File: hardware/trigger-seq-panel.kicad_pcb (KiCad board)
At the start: 2 copper layers, 80.8 x 104.6 mm, 102 parts, among them J1 CLOCK_IN, J2 RESET, J3 DIRECTION, J4 OUT 1, J5 OUT 2, J6 CLOCK_OUT, J7 RUN/STOP, P2 COUNT_PANEL, P4 CLOCK_PANEL, P6 SWITCH_PANEL, P9 OUTS_PANEL, SW1 RESET, SW10 SWITCH_INV, SW11 SWITCH_INV, SW12 SWITCH_INV, SW13 SWITCH_INV, SW14 SWITCH_INV, SW15 SWITCH_INV, SW16 SWITCH_INV, SW17 SWITCH_INV, SW18 SWITCH_INV, SW19 SWITCH_INV, SW2 UP/DOWN, SW20 RUN/STOP, SW3 SW_DPDT_x2, SW4 SWITCH_INV, SW5 SWITCH_INV, SW6 SWITCH_INV, SW7 SWITCH_INV, SW8 SWITCH_INV, SW9 SWITCH_INV

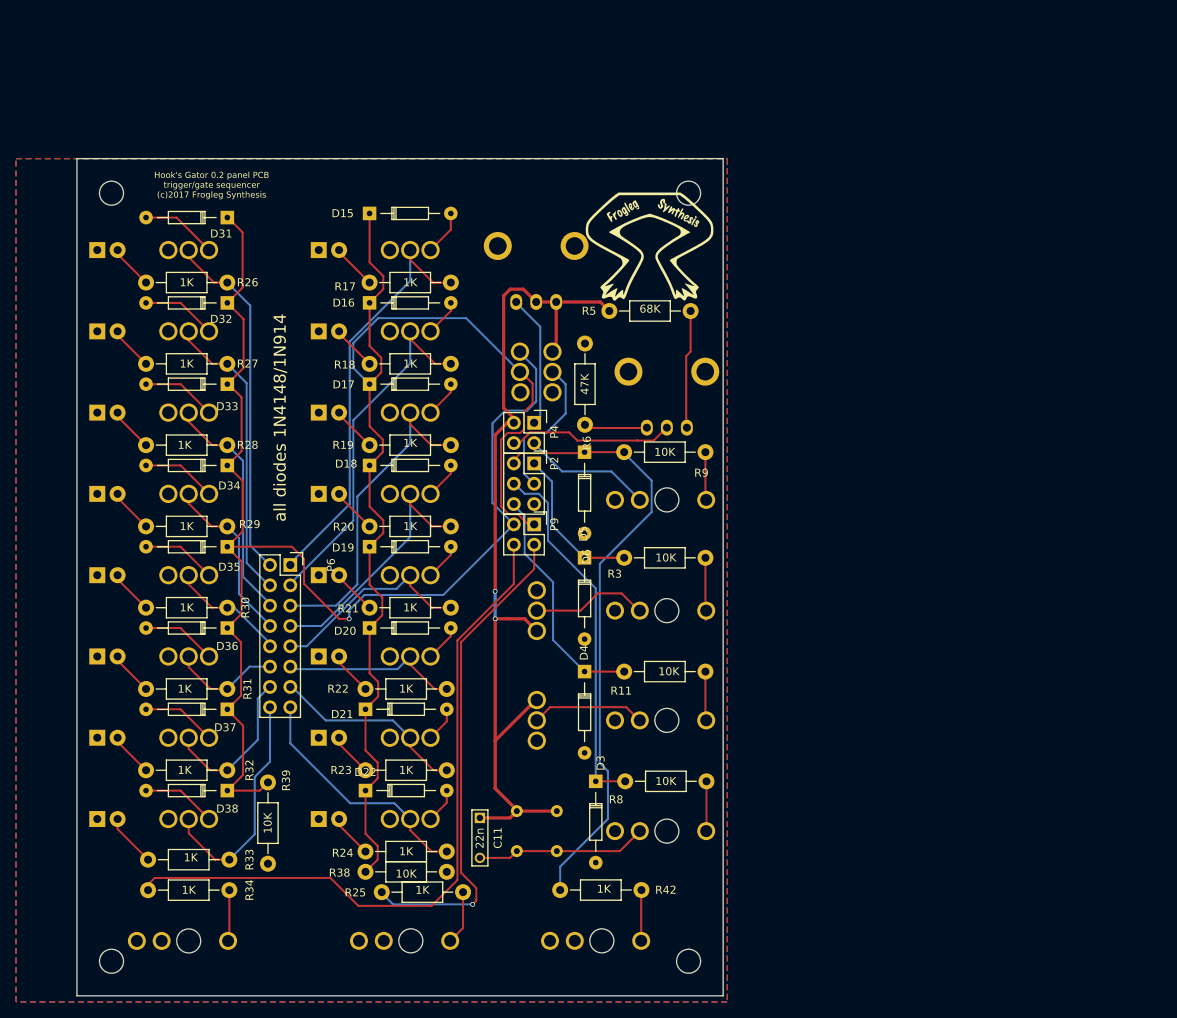
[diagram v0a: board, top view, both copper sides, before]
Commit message: replaced old hardware files with the most recent ones tracking CLAUDE.md AI files used in revising the project
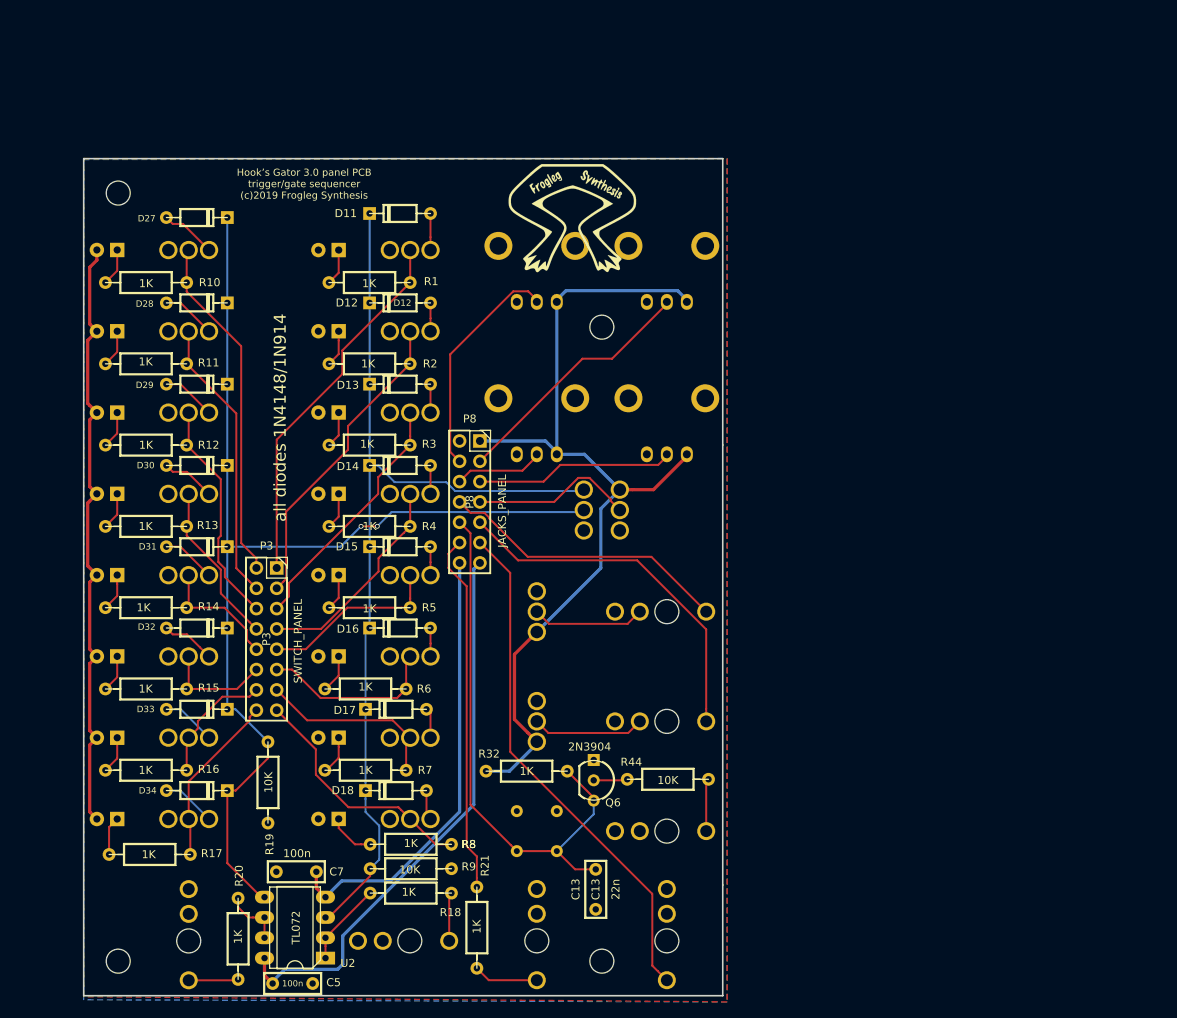
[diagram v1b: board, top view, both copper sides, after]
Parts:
- removed C11: 22n, Capacitors_ThroughHole:C_Rect_L7_W2_P5
- removed D35, D36, D37, D38: 1N4148, Diodes_ThroughHole:Diode_DO-35_SOD27_Horizontal_RM10
- removed P2: COUNT_PANEL, Socket_Strips:Socket_Strip_Straight_2x03
- removed P4: CLOCK_PANEL, Socket_Strips:Socket_Strip_Straight_2x02
- removed P6: SWITCH_PANEL, Socket_Strips:Socket_Strip_Straight_2x08
- removed P9: OUTS_PANEL, Socket_Strips:Socket_Strip_Straight_2x02
- removed R22, R23, R24, R25, R26, R27, R28, R29, R30, R31, R33, R34, R42: 1K, Resistors_ThroughHole:Resistor_Horizontal_RM10mm
- removed R38, R39: 10K, Resistors_ThroughHole:Resistor_Horizontal_RM10mm
- removed the SW14 at (86.8, 84.3)
- added C13: 22n, Capacitor_THT:C_Disc_D7.0mm_W2.5mm_P5.00mm, F.Cu at (137.7, 146.4)
- added C5: 100n, Capacitor_THT:C_Disc_D7.0mm_W2.5mm_P5.00mm, F.Cu at (97.3, 155.7)
- added C7: 100n, Capacitor_THT:C_Disc_D7.0mm_W2.5mm_P5.00mm, F.Cu at (102.7, 141.7)
- added P3: SWITCH_PANEL, Connector_PinSocket_2.54mm:PinSocket_2x08_P2.54mm_Vertical, F.Cu at (97.8, 103.8)
- added P8: JACKS_PANEL, Connector_PinSocket_2.54mm:PinSocket_2x07_P2.54mm_Vertical, F.Cu at (123.2, 87.9)
- added Q6: 2N3904, Package_TO_SOT_THT:TO-92_Inline_Wide, F.Cu at (137.4, 127.8)
- added R1: 1K, Resistor_THT:R_Axial_DIN0207_L6.3mm_D2.5mm_P10.16mm_Horizontal, F.Cu at (114.5, 68.1)
- added R10: 1K, Resistor_THT:R_Axial_DIN0207_L6.3mm_D2.5mm_P10.16mm_Horizontal, F.Cu at (86.5, 68.1)
- added R12: 1K, Resistor_THT:R_Axial_DIN0207_L6.3mm_D2.5mm_P10.16mm_Horizontal, F.Cu at (86.5, 88.4)
- added R13: 1K, Resistor_THT:R_Axial_DIN0207_L6.3mm_D2.5mm_P10.16mm_Horizontal, F.Cu at (86.5, 98.6)
- added R14: 1K, Resistor_THT:R_Axial_DIN0207_L6.3mm_D2.5mm_P10.16mm_Horizontal, F.Cu at (86.5, 108.7)
- added R15: 1K, Resistor_THT:R_Axial_DIN0207_L6.3mm_D2.5mm_P10.16mm_Horizontal, F.Cu at (86.5, 118.9)
- added R16: 1K, Resistor_THT:R_Axial_DIN0207_L6.3mm_D2.5mm_P10.16mm_Horizontal, F.Cu at (86.5, 129.0)
- added R2: 1K, Resistor_THT:R_Axial_DIN0207_L6.3mm_D2.5mm_P10.16mm_Horizontal, F.Cu at (114.5, 78.2)
- added R4: 1K, Resistor_THT:R_Axial_DIN0207_L6.3mm_D2.5mm_P10.16mm_Horizontal, F.Cu at (114.5, 98.6)
- added R44: 10K, Resistor_THT:R_Axial_DIN0207_L6.3mm_D2.5mm_P10.16mm_Horizontal, F.Cu at (141.6, 130.2)
- added R7: 1K, Resistor_THT:R_Axial_DIN0207_L6.3mm_D2.5mm_P10.16mm_Horizontal, F.Cu at (114.0, 129.0)
- added RV3: STEPS, Walter Resistors:trimmer_alps-rk09k1130ah1, B.Cu at (146.6, 82.5)
- added RV4: SWING, Walter Resistors:trimmer_alps-rk09k1130ah1, B.Cu at (130.3, 82.5)
- added SW16: SW_SPDT, My Library:submini_toggle_SPDT_2267079, B.Cu at (86.8, 125.0)
- added U2: TL072, Package_DIP:DIP-8_W7.62mm_LongPads, F.Cu at (103.9, 152.5)
- D10: value S4 -> S8; footprint LEDs:LED-3MM -> My Library:LED_D3.0mm
- D11: value S5 -> 1N4148; footprint LEDs:LED-3MM -> Diode_THT:D_DO-35_SOD27_P7.62mm_Horizontal; moved to F.Cu
- D12: value S6 -> 1N4148; footprint LEDs:LED-3MM -> Diode_THT:D_DO-35_SOD27_P7.62mm_Horizontal; moved to F.Cu
- D13: value S7 -> 1N4148; footprint LEDs:LED-3MM -> Diode_THT:D_DO-35_SOD27_P7.62mm_Horizontal; moved to F.Cu
- D14: value S8 -> 1N4148; footprint LEDs:LED-3MM -> Diode_THT:D_DO-35_SOD27_P7.62mm_Horizontal; moved to F.Cu
- D15, D16, D17, D18, D31, D32, D33, D34: footprint Diodes_ThroughHole:Diode_DO-35_SOD27_Horizontal_RM10 -> Diode_THT:D_DO-35_SOD27_P7.62mm_Horizontal
- D19: value 1N4148 -> S9; footprint Diodes_ThroughHole:Diode_DO-35_SOD27_Horizontal_RM10 -> My Library:LED_D3.0mm; moved to B.Cu
- D20: value 1N4148 -> S10; footprint Diodes_ThroughHole:Diode_DO-35_SOD27_Horizontal_RM10 -> My Library:LED_D3.0mm; moved to B.Cu
- D21: value 1N4148 -> S11; footprint Diodes_ThroughHole:Diode_DO-35_SOD27_Horizontal_RM10 -> My Library:LED_D3.0mm; moved to B.Cu
- D22: value 1N4148 -> S12; footprint Diodes_ThroughHole:Diode_DO-35_SOD27_Horizontal_RM10 -> My Library:LED_D3.0mm; moved to B.Cu
- D23: value S9 -> S13; footprint LEDs:LED-3MM -> My Library:LED_D3.0mm
- D24: value S10 -> S14; footprint LEDs:LED-3MM -> My Library:LED_D3.0mm
- D25: value S11 -> S15; footprint LEDs:LED-3MM -> My Library:LED_D3.0mm
- D26: value S12 -> S16; footprint LEDs:LED-3MM -> My Library:LED_D3.0mm
- D27: value S13 -> 1N4148; footprint LEDs:LED-3MM -> Diode_THT:D_DO-35_SOD27_P7.62mm_Horizontal; moved to F.Cu
- D28: value S14 -> 1N4148; footprint LEDs:LED-3MM -> Diode_THT:D_DO-35_SOD27_P7.62mm_Horizontal; moved to F.Cu
- D29: value S15 -> 1N4148; footprint LEDs:LED-3MM -> Diode_THT:D_DO-35_SOD27_P7.62mm_Horizontal; moved to F.Cu
- D3: value 1N4148 -> S1; footprint Diodes_ThroughHole:Diode_DO-35_SOD27_Horizontal_RM10 -> My Library:LED_D3.0mm; moved to B.Cu
- D30: value S16 -> 1N4148; footprint LEDs:LED-3MM -> Diode_THT:D_DO-35_SOD27_P7.62mm_Horizontal; moved to F.Cu
- D4: value 1N4148 -> S2; footprint Diodes_ThroughHole:Diode_DO-35_SOD27_Horizontal_RM10 -> My Library:LED_D3.0mm; moved to B.Cu
- D5: value 1N4148 -> S3; footprint Diodes_ThroughHole:Diode_DO-35_SOD27_Horizontal_RM10 -> My Library:LED_D3.0mm; moved to B.Cu
- D6: value 1N4148 -> S4; footprint Diodes_ThroughHole:Diode_DO-35_SOD27_Horizontal_RM10 -> My Library:LED_D3.0mm; moved to B.Cu
- D7: value S1 -> S5; footprint LEDs:LED-3MM -> My Library:LED_D3.0mm
- D8: value S2 -> S6; footprint LEDs:LED-3MM -> My Library:LED_D3.0mm
- D9: value S3 -> S7; footprint LEDs:LED-3MM -> My Library:LED_D3.0mm
- J1: value CLOCK_IN -> OUT1
- J2: value RESET -> OUT2
- J3: value DIRECTION -> RESET
- J4: value OUT 1 -> CLOCK_IN
- J5: value OUT 2 -> RUN_STOP
- J6: value CLOCK_OUT -> UP_DOWN
- J7: value RUN/STOP -> CLOCK_OUT
- R11, R3, R8: value 10K -> 1K; footprint Resistors_ThroughHole:Resistor_Horizontal_RM10mm -> Resistor_THT:R_Axial_DIN0207_L6.3mm_D2.5mm_P10.16mm_Horizontal
- R17, R18, R20, R21, R32, R9: footprint Resistors_ThroughHole:Resistor_Horizontal_RM10mm -> Resistor_THT:R_Axial_DIN0207_L6.3mm_D2.5mm_P10.16mm_Horizontal
- R19: value 1K -> 10K; footprint Resistors_ThroughHole:Resistor_Horizontal_RM10mm -> Resistor_THT:R_Axial_DIN0207_L6.3mm_D2.5mm_P10.16mm_Horizontal
- R5: value 68K -> 1K; footprint Resistors_ThroughHole:Resistor_Horizontal_RM10mm -> Resistor_THT:R_Axial_DIN0207_L6.3mm_D2.5mm_P10.16mm_Horizontal
- R6: value 47K -> 1K; footprint Resistors_ThroughHole:Resistor_Horizontal_RM10mm -> Resistor_THT:R_Axial_DIN0207_L6.3mm_D2.5mm_P10.16mm_Horizontal
- RV1: value 100K -> RATE
- RV2: value 100K -> WIDTH
- SW1: value RESET -> SW_SPDT; footprint My Library:C&K_round_pushbutton -> My Library:submini_toggle_SPDT_2267079
- SW10, SW11, SW12, SW13, SW15, SW17, SW4, SW5, SW6, SW7, SW8: value SWITCH_INV -> SW_SPDT
- SW14: renamed from SW16; value SWITCH_INV -> SW_SPDT
- SW18: value SWITCH_INV -> Run/Stop
- SW19: value SWITCH_INV -> Up/Down
- SW2: value UP/DOWN -> SW_SPDT
- SW20: value RUN/STOP -> RESET; footprint My Library:submini_toggle_SPDT_2267079 -> My Library:C&K_round_pushbutton
- SW3: value SW_DPDT_x2 -> SW_SPDT; footprint My Library:submini_toggle_DPDT_2267079 -> My Library:submini_toggle_SPDT_2267079
- SW9: value SWITCH_INV -> SW_DPDT_x2; footprint My Library:submini_toggle_SPDT_2267079 -> My Library:submini_toggle_DPDT_wider
- moved R17 76.6 mm to (87.0, 139.6)
- moved SW1 74.3 mm to (114.5, 64.0), turned to -90 degrees
- moved D3 74.3 mm to (104.3, 64.0), turned to 0 degrees
- moved J5 72.6 mm to (146.6, 109.2)
- moved SW10 67.0 mm to (86.8, 64.0)
- moved SW11 67.0 mm to (86.8, 74.2)
- moved R11 66.9 mm to (86.5, 78.2), turned to 180 degrees
- moved R18 66.4 mm to (119.6, 144.4)
- moved J1 63.8 mm to (114.4, 150.4)
- moved J2 61.3 mm to (86.8, 150.4), turned to 0 degrees
- moved R20 60.6 mm to (93.0, 155.2), turned to 90 degrees
- moved R9 56.4 mm to (119.6, 141.4), turned to 180 degrees
- moved D4 53.2 mm to (104.3, 74.2), turned to 0 degrees
- moved SW2 51.1 mm to (114.5, 74.2), turned to -90 degrees
- moved R19 50.5 mm to (96.7, 135.6), turned to 90 degrees
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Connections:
- D11 pad 1: GND -> Net-(D11-Pad1)
- D12 pad 1: GND -> Net-(D11-Pad1)
- D13 pad 1: GND -> Net-(D11-Pad1)
- D14 pad 1: GND -> Net-(D11-Pad1)
- D15 pad 1: /main/counter/1ST8 -> Net-(D11-Pad1)
- D16 pad 1: /main/counter/1ST8 -> Net-(D11-Pad1)
- D17 pad 1: /main/counter/1ST8 -> Net-(D11-Pad1)
- D18 pad 1: /main/counter/1ST8 -> Net-(D11-Pad1)
- D19 pad 1: /main/counter/1ST8 -> GND
- D20 pad 1: /main/counter/1ST8 -> GND
- D21 pad 1: /main/counter/1ST8 -> GND
- D22 pad 1: /main/counter/1ST8 -> GND
- D27 pad 1: GND -> Net-(D27-Pad1)
- D28 pad 1: GND -> Net-(D27-Pad1)
- D29 pad 1: GND -> Net-(D27-Pad1)
- D3 pad 1: /main/counter/reset processing/reset.in -> GND
- D3 pad 2: GND -> Net-(D3-Pad2)
- D30 pad 1: GND -> Net-(D27-Pad1)
- D31 pad 1: /main/counter/2ND8 -> Net-(D27-Pad1)
- D32 pad 1: /main/counter/2ND8 -> Net-(D27-Pad1)
- D33 pad 1: /main/counter/2ND8 -> Net-(D27-Pad1)
- D34 pad 1: /main/counter/2ND8 -> Net-(D27-Pad1)
- D4 pad 1: Net-(D4-Pad1) -> GND
- D4 pad 2: GND -> Net-(D4-Pad2)
- D5 pad 1: Net-(D5-Pad1) -> GND
- D5 pad 2: GND -> Net-(D5-Pad2)
- D6 pad 1: /main/counter/PROC_CLK -> GND
- D6 pad 2: GND -> Net-(D6-Pad2)
- J1 pad 2: /main/clock/INT_CLK -> (no net)
- J2 pad 2: Net-(C11-Pad2) -> (no net)
- J3 pad 2: Net-(J3-Pad2) -> GND
- J4 pad 1: Net-(J4-Pad1) -> CKIN
- J4 pad 2: (no net) -> GND
- J5 pad 1: Net-(J5-Pad1) -> R/S
- J5 pad 2: (no net) -> Net-(J5-Pad2)
- J6 pad 1: Net-(J6-Pad1) -> U/D
- J6 pad 2: (no net) -> Net-(J6-Pad2)
- J7 pad 2: Net-(J7-Pad2) -> (no net)
- R11 pad 1: Net-(D4-Pad1) -> /main/outputs/S10
- R11 pad 2: Net-(J3-Pad1) -> Net-(D20-Pad2)
- R17 pad 1: /main/counter/S1 -> /main/outputs/S16
- R17 pad 2: Net-(D7-Pad2) -> Net-(D26-Pad2)
- R18 pad 1: /main/counter/S2 -> Net-(J1-Pad1)
- R18 pad 2: Net-(D8-Pad2) -> Net-(R18-Pad2)
- R19 pad 1: /main/counter/S3 -> GND
- R19 pad 2: Net-(D9-Pad2) -> Net-(D27-Pad1)
- R20 pad 1: /main/counter/S4 -> Net-(J2-Pad1)
- R20 pad 2: Net-(D10-Pad2) -> Net-(R20-Pad2)
- R21 pad 1: /main/counter/S5 -> /main/clock/ckbuf
- R21 pad 2: Net-(D11-Pad2) -> Net-(J7-Pad1)
- R3 pad 1: Net-(D5-Pad1) -> /main/outputs/S3
- R3 pad 2: Net-(J7-Pad1) -> Net-(D5-Pad2)
- R32 pad 1: /main/counter/S15 -> +5V
- R32 pad 2: Net-(D29-Pad2) -> reset
- R5 pad 1: Net-(R5-Pad1) -> /main/outputs/S5
- R5 pad 2: +12V -> Net-(D7-Pad2)
- R6 pad 1: GND -> /main/outputs/S6
- R6 pad 2: Net-(R6-Pad2) -> Net-(D8-Pad2)
- R8 pad 1: /main/counter/reset processing/reset.in -> /main/outputs/S8
- R8 pad 2: Net-(J2-Pad1) -> Net-(D10-Pad2)
- R9 pad 1: /main/counter/PROC_CLK -> GND
- R9 pad 2: Net-(J1-Pad1) -> Net-(D11-Pad1)
- RV1 pad 1: +12V -> +5V
- RV1 pad 2: +12V -> rate
- RV1 pad 3: Net-(P4-Pad1) -> GND
- RV2 pad 1: Net-(R5-Pad1) -> +5V
- RV2 pad 2: Net-(P4-Pad4) -> width
- RV2 pad 3: Net-(R6-Pad2) -> GND
- SW1 pad 1: Net-(C11-Pad2) -> Net-(D11-Pad2)
- SW1 pad 2: +12V -> /main/outputs/S1
- SW10 pad 1: Net-(D21-Pad2) -> Net-(D27-Pad2)
- SW10 pad 2: /main/counter/S7 -> /main/outputs/S9
- SW11 pad 1: Net-(D22-Pad2) -> Net-(D28-Pad2)
- SW11 pad 2: /main/counter/S8 -> /main/outputs/S10
- SW12 pad 1: Net-(D31-Pad2) -> Net-(D29-Pad2)
- SW12 pad 2: /main/counter/S9 -> /main/outputs/S11
- SW13 pad 1: Net-(D32-Pad2) -> Net-(D30-Pad2)
- SW13 pad 2: /main/counter/S10 -> /main/outputs/S12
- SW14 pad 1: Net-(D35-Pad2) -> Net-(D31-Pad2)
- SW14 pad 2: /main/counter/S13 -> /main/outputs/S13
- SW15 pad 1: Net-(D34-Pad2) -> Net-(D32-Pad2)
- SW15 pad 2: /main/counter/S12 -> /main/outputs/S14
- SW17 pad 1: Net-(D36-Pad2) -> Net-(D34-Pad2)
- SW17 pad 2: /main/counter/S14 -> /main/outputs/S16
- SW18 pad 1: Net-(D37-Pad2) -> GND
- SW18 pad 2: /main/counter/S15 -> Net-(J5-Pad2)
- SW18 pad 3: (no net) -> +5V
- SW19 pad 1: Net-(D38-Pad2) -> +5V
- SW19 pad 2: /main/counter/S16 -> Net-(J6-Pad2)
- SW19 pad 3: (no net) -> GND
- SW2 pad 1: GND -> Net-(D12-Pad2)
- SW2 pad 2: Net-(J3-Pad2) -> /main/outputs/S2
- SW2 pad 3: +12V -> (no net)
- SW20 pad 1: GND -> reset
- SW20 pad 2: Net-(J7-Pad2) -> GND
- SW3 pad 1: +12V -> Net-(D13-Pad2)
- SW3 pad 2: Net-(P2-Pad3) -> /main/outputs/S3
- SW3 pad 3: GND -> (no net)
- SW4 pad 1: Net-(D15-Pad2) -> Net-(D14-Pad2)
- SW4 pad 2: /main/counter/S1 -> /main/outputs/S4
- SW5 pad 1: Net-(D16-Pad2) -> Net-(D15-Pad2)
- SW5 pad 2: /main/counter/S2 -> /main/outputs/S5
- SW6 pad 1: Net-(D17-Pad2) -> Net-(D16-Pad2)
- SW6 pad 2: /main/counter/S3 -> /main/outputs/S6
- SW7 pad 1: Net-(D18-Pad2) -> Net-(D17-Pad2)
- SW7 pad 2: /main/counter/S4 -> /main/outputs/S7
- SW8 pad 1: Net-(D19-Pad2) -> Net-(D18-Pad2)
- SW8 pad 2: /main/counter/S5 -> /main/outputs/S8
- SW9 pad 1: Net-(D20-Pad2) -> +5V
- SW9 pad 2: /main/counter/S6 -> 2x8/1x16
- SW9 pad 3: (no net) -> GND
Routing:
- net /main/counter/2ND8: track 162.4 -> 0.00 mm, vias 1 -> 0
- net /main/counter/1ST8: track 148.5 -> 0.00 mm
- net Net-(D27-Pad1): track 0.00 -> 139.0 mm, vias 0 -> 2
- net Net-(D11-Pad1): track 0.00 -> 120.1 mm
- net +5V: track 0.00 -> 113.2 mm
- net Net-(P10-Pad4): track 87.3 -> 0.00 mm
- net /main/counter/PROC_CLK: track 77.1 -> 0.00 mm
- net GND: track 0.00 -> 76.8 mm
- net reset: track 0.00 -> 68.2 mm
- net CKIN: track 0.00 -> 64.4 mm
- net Net-(P10-Pad3): track 61.8 -> 0.00 mm, vias 1 -> 0
- net -12V: track 0.00 -> 55.8 mm
- net /main/counter/S1: track 53.0 -> 0.00 mm
- net /main/counter/reset processing/reset.in: track 46.9 -> 0.00 mm
- net /main/outputs/S1: track 0.00 -> 46.7 mm
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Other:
- board size 80.8 x 104.6 mm -> 79.9 x 104.6 mm
- net class Default removed
- net class power removed
- board text added: "Hook’s Gator 3.0 panel PCB trigger/gate sequencer (c)2019 Frogleg Synthesis"
- board text added: "all pots 10kB"
- board text added: "steps"
- board text added: "swing"
- board text removed: "Hook's Gator 0.2 panel PCB trigger/gate sequencer (c)2017 Frogleg Synthesis"

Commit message: expanding panel to 18HP so the controls are less crowded
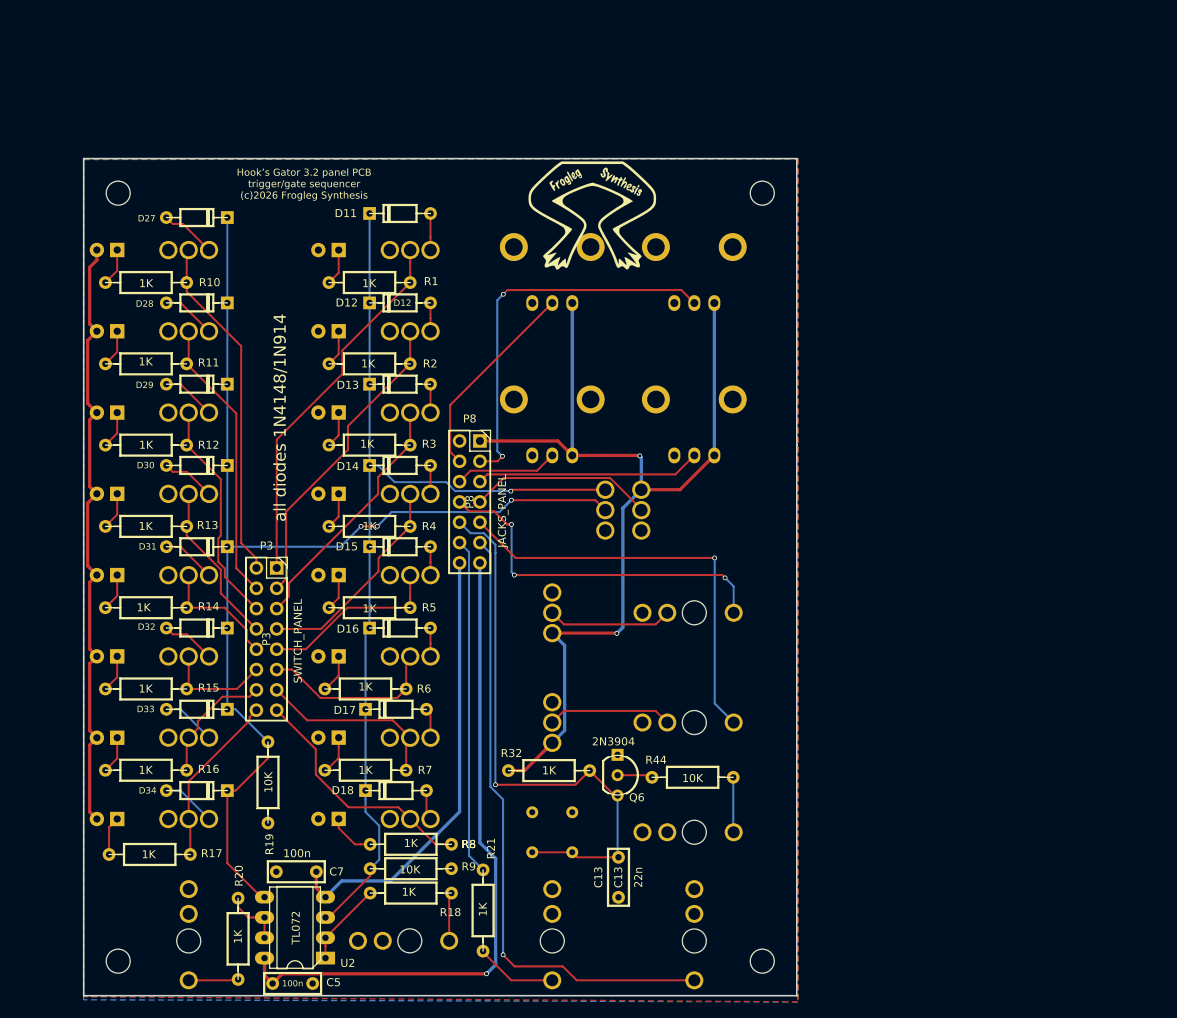
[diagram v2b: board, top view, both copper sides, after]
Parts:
- moved REF** 26.1 mm to (158.5, 56.9)
- moved REF** 20.1 mm to (158.5, 152.9)
- moved RV3 3.44 mm to (150.0, 82.7)
- moved J3 3.44 mm to (150.0, 136.8)
- moved J5 3.44 mm to (150.0, 109.4)
- moved RV2 3.44 mm to (150.0, 63.6)
- moved J6 3.44 mm to (150.0, 123.1)
- moved J4 3.43 mm to (150.0, 150.4)
- moved C13 3.22 mm to (140.5, 144.9)
- moved R44 3.10 mm to (144.7, 129.9)
- moved Q6 3.05 mm to (140.4, 127.1)
- moved R32 2.80 mm to (126.8, 129.1)
- moved SW9 2.68 mm to (141.1, 96.5)
- moved G*** 2.52 mm to (137.2, 60.4)
- moved R21 2.28 mm to (123.6, 141.5)
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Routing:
- net width: track 31.8 -> 48.7 mm, vias 0 -> 2
- net CKIN: track 64.4 -> 78.0 mm, vias 0 -> 1
- net +12V: track 70.5 -> 83.3 mm, vias 0 -> 1
- net +5V: track 113.2 -> 123.3 mm, vias 0 -> 2
- net R/S: track 36.6 -> 45.4 mm, vias 0 -> 3
- net U/D: track 45.3 -> 52.8 mm, vias 0 -> 1
- net Net-(D27-Pad1): track 139.0 -> 142.7 mm, vias 2 -> 3
- net reset: track 68.2 -> 71.7 mm, vias 0 -> 1
- net steps: track 24.9 -> 28.2 mm
- net rate: track 28.6 -> 25.6 mm
- net /main/clock/ckbuf: track 45.1 -> 42.1 mm
- net Net-(D11-Pad1): track 120.1 -> 122.8 mm, vias 0 -> 1
- net 2x8/1x16: track 20.5 -> 23.1 mm
- net Net-(J7-Pad1): track 8.11 -> 10.2 mm
- net swing: track 11.2 -> 12.9 mm
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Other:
- board size 79.9 x 104.6 mm -> 89.1 x 104.6 mm
- board text added: "Hook’s Gator 3.2 panel PCB trigger/gate sequencer (c)2026 Frogleg Synthesis"
- board text removed: "Hook’s Gator 3.0 panel PCB trigger/gate sequencer (c)2019 Frogleg Synthesis"

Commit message: wider panel + better spacing v3.3
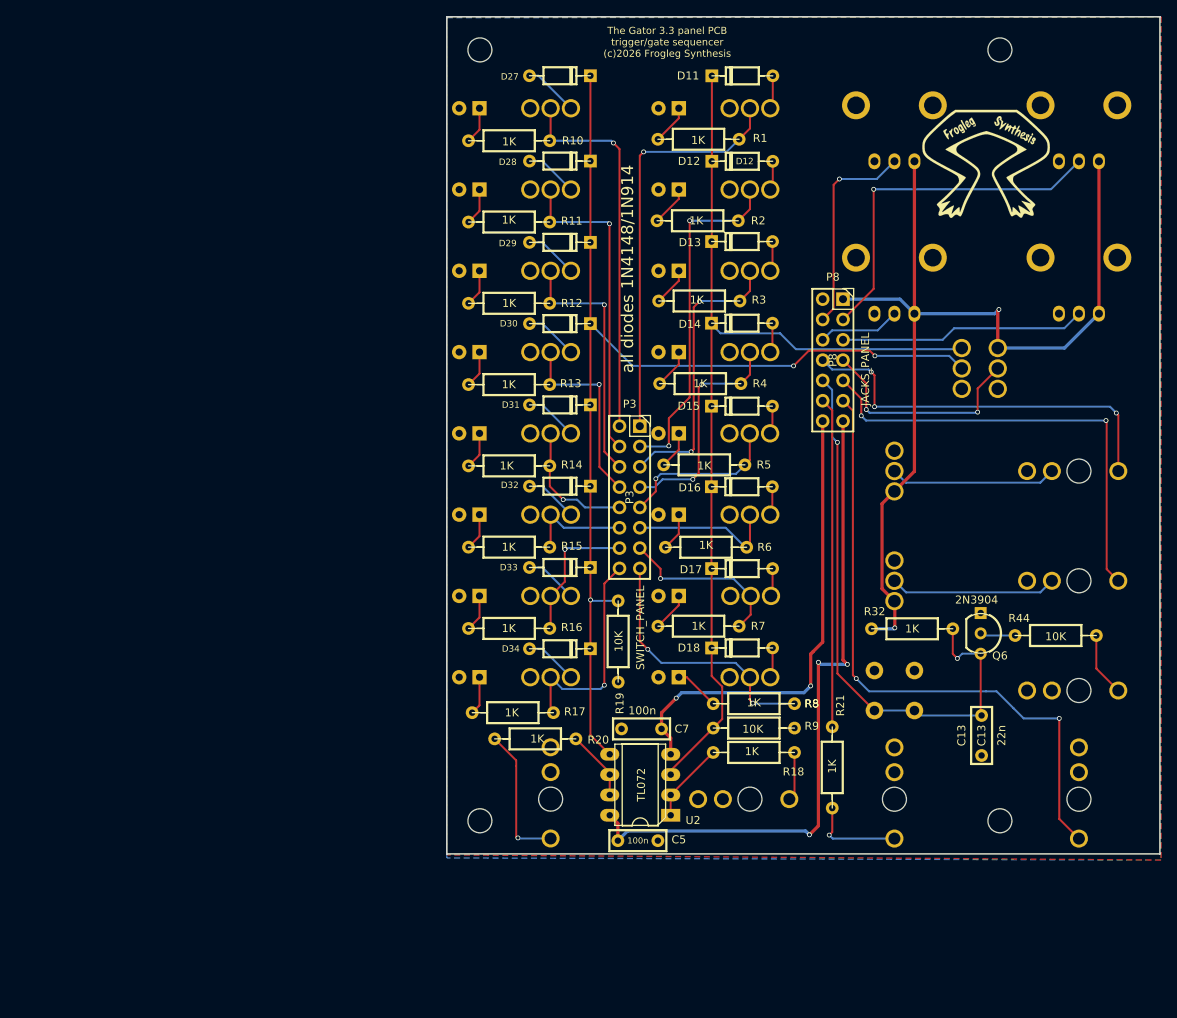
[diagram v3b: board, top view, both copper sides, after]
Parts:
- SW20: footprint My Library:C&K_round_pushbutton -> myfootprints:C&K_round_pushbutton
- moved RV3 51.2 mm to (198.1, 65.0)
- moved RV2 51.2 mm to (198.1, 45.9)
- moved J4 51.2 mm to (198.1, 132.7)
- moved J3 51.2 mm to (198.1, 119.1)
- moved J5 51.2 mm to (198.1, 91.6)
- moved J6 51.2 mm to (198.1, 105.4)
- moved G*** 49.6 mm to (186.5, 53.9)
- moved Q6 48.7 mm to (185.8, 109.4)
- moved D27 48.7 mm to (137.0, 42.2)
- moved D28 48.7 mm to (137.0, 52.9)
- moved D29 48.7 mm to (137.0, 63.1)
- moved D30 48.7 mm to (137.0, 73.2)
- moved D31 48.7 mm to (137.0, 83.4)
- moved D33 48.7 mm to (137.0, 103.7)
- moved D34 48.7 mm to (137.0, 113.9)
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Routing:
- net GND: track 76.8 -> 0.00 mm
- net Net-(J2-Pad1): track 6.22 -> 17.8 mm, vias 0 -> 1
- net /main/outputs/S16: track 21.6 -> 27.5 mm, vias 0 -> 1
- net Net-(J6-Pad2): track 15.6 -> 20.9 mm
- net Net-(J5-Pad2): track 15.6 -> 20.9 mm
- net /main/outputs/S1: track 46.7 -> 51.5 mm, vias 0 -> 1
- net 2x8/1x16: track 23.1 -> 28.0 mm, vias 0 -> 2
- net /main/outputs/S2: track 39.0 -> 43.5 mm, vias 0 -> 2
- net /main/outputs/S9: track 43.5 -> 47.9 mm, vias 0 -> 1
- net /main/outputs/S3: track 31.4 -> 35.8 mm, vias 0 -> 2
- net U/D: track 52.8 -> 57.1 mm, vias 1 -> 2
- net /main/outputs/S10: track 35.8 -> 40.0 mm, vias 0 -> 1
- net /main/outputs/S6: track 22.4 -> 18.6 mm
- net width: track 48.7 -> 45.0 mm, vias 2 -> 1
- net R/S: track 45.4 -> 49.1 mm
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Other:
- outline, holes or cut-outs redrawn
- board text added: "The Gator 3.3 panel PCB trigger/gate sequencer (c)2026 Frogleg Synthesis"
- board text removed: "Hook’s Gator 3.2 panel PCB trigger/gate sequencer (c)2026 Frogleg Synthesis"
